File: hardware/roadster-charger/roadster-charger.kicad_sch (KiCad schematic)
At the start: 54 parts, among them J1 USB4505-03-0-A, J2 USB4505-03-0-A, J3 54-00166, Q1 CSD19532Q5B, U1 FUSB307BMPX, U10 OPA340NA, U11 LM75B, U2 ESP32-C3-MINI-1, U3 INA168, U4 LM5050-1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

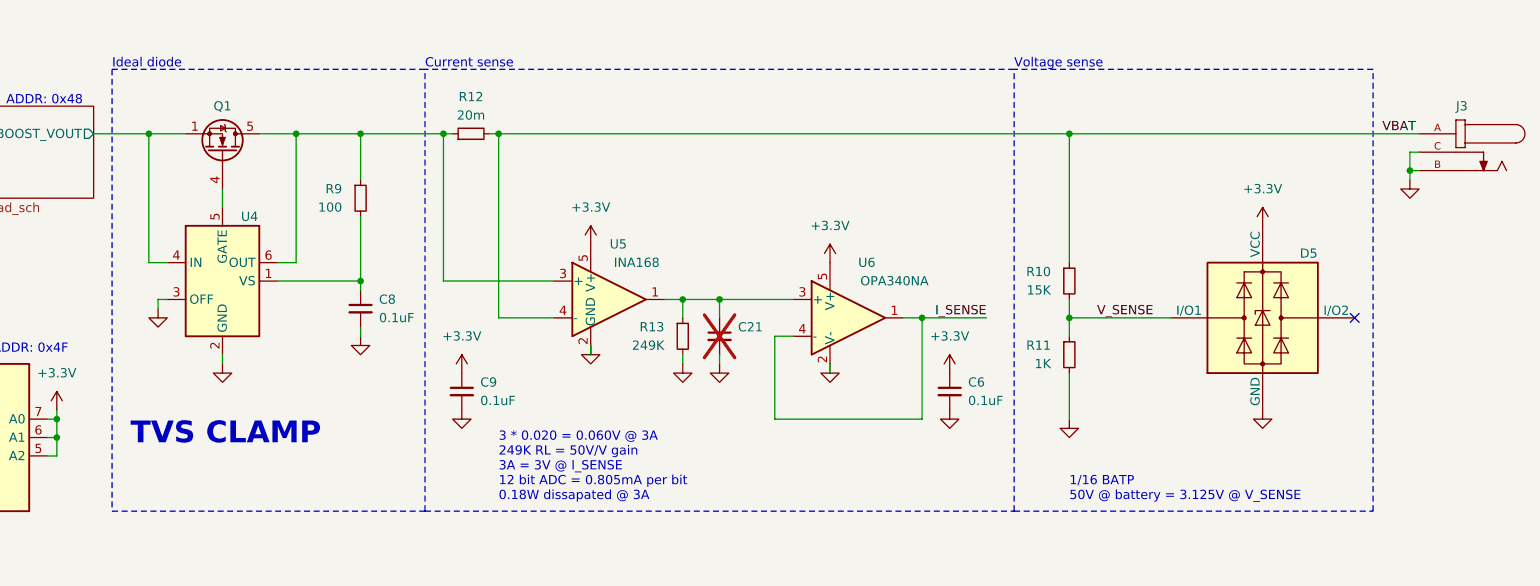
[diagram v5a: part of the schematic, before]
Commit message: add output transient suppressor
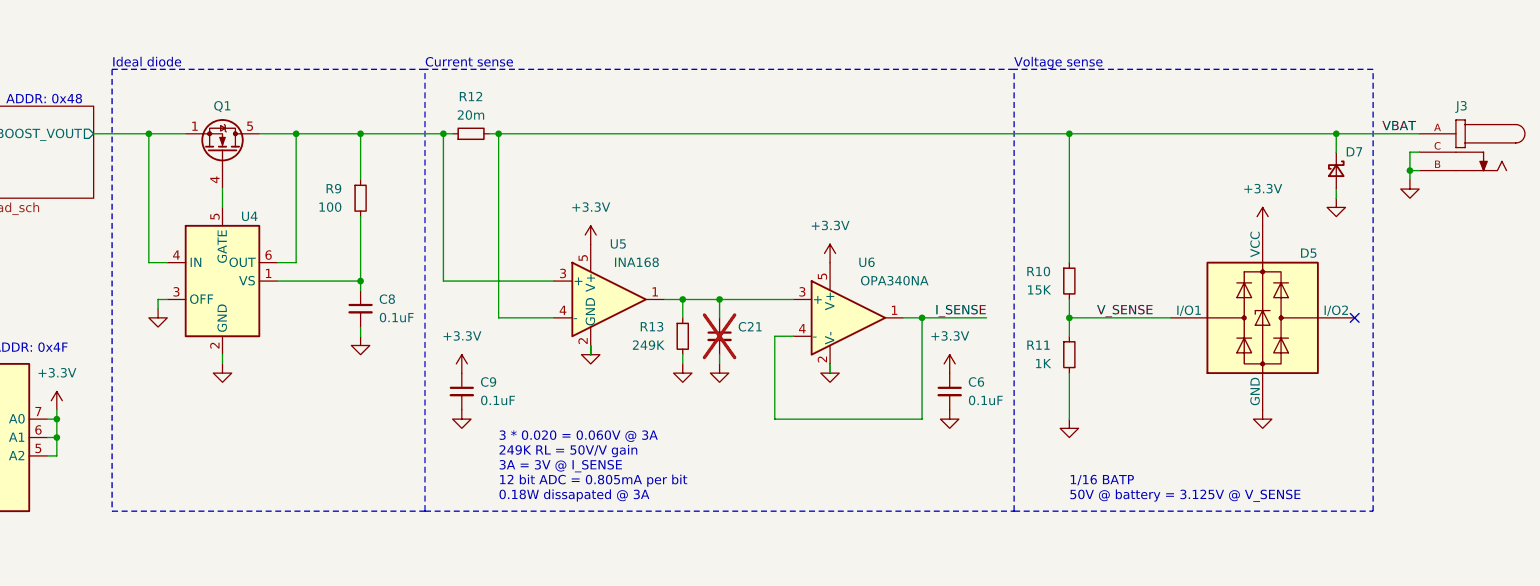
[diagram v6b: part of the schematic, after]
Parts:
- added D7: D_Schottky_Small, Diode_SMD:D_SMB, symbol Device:D_Schottky_Small
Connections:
- net GND: now also D7.2 (A)
- net VBAT: now also D7.1 (K)
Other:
- note removed: "TVS CLAMP"
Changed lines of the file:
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@@
   (junction (at 161.29 138.43) (diameter 0) (color 0 0 0 0)
   )
+  (junction (at 377.19 138.43) (diameter 0) (color 0 0 0 0)
+  )
   (junction (at 290.83 31.75) (diameter 0) (color 0 0 0 0)
   )
@@
     (stroke (width 0) (type default))
   )
+  (wire (pts (xy 377.19 138.43) (xy 388.62 138.43))
+    (stroke (width 0) (type default))
+  )
   (wire (pts (xy 36.83 124.46) (xy 36.83 125.73))
     (stroke (width 0) (type default))
@@
     (stroke (width 0) (type default))
   )
-  (wire (pts (xy 340.36 138.43) (xy 388.62 138.43))
+  (wire (pts (xy 340.36 138.43) (xy 377.19 138.43))
     (stroke (width 0) (type default))
   )
@@
     (stroke (width 0) (type default))
   )
+  (wire (pts (xy 377.19 138.43) (xy 377.19 140.97))
+    (stroke (width 0) (type default))
+  )
   (wire (pts (xy 96.52 222.25) (xy 109.22 222.25))
     (stroke (width 0) (type default))
@@
     (stroke (width 0) (type default))
   )
+  (wire (pts (xy 377.19 146.05) (xy 377.19 147.32))
+    (stroke (width 0) (type default))
+  )
   (wire (pts (xy 292.1 63.5) (xy 292.1 66.04))
     (stroke (width 0) (type default))
@@
     (effects (font (size 1.27 1.27)) (justify left bottom))
   )
-  (text "TVS CLAMP" (at 210.82 181.61 0)
-    (effects (font (size 3 3) (thickness 0.6) bold (color 255 22 22 1)) (justify left bottom))
-  )
   (text "1/16 BATP\n50V @ battery = 3.125V @ V_SENSE" (at 340.36 189.23 0)
     (effects (font (size 1.27 1.27)) (justify left bottom))
@@
     )
   )
+  (symbol (lib_id "power:GND") (at 377.19 147.32 0) (unit 1)
+    (in_bom yes) (on_board yes) (dnp no)
+    (property "Reference" "#PWR079" (at 377.19 153.67 0)
+      (effects (font (size 1.27 1.27)) hide)
+    )
+    (property "Value" "GND" (at 377.19 152.4 0)
+      (effects (font (size 1.27 1.27)) hide)
+    )
+    (property "Footprint" "" (at 377.19 147.32 0)
+      (effects (font (size 1.27 1.27)) hide)
+    )
+    (property "Datasheet" "" (at 377.19 147.32 0)
+      (effects (font (size 1.27 1.27)) hide)
+    )
+    (pin "1")
+    (instances
+      (project "roadster-charger"
+        (path "/57ecac41-cd8a-4182-a81e-fed3e381aedd"
+          (reference "#PWR079") (unit 1)
+        )
+        (path "/57ecac41-cd8a-4182-a81e-fed3e381aedd/64ca4e4e-11ba-4e5c-8f8e-2432a1d47dd0"
+          (reference "#PWR028") (unit 1)
+        )
+      )
+    )
+  )
   (symbol (lib_id "Sensor_Temperature:LM75B") (at 189.23 180.34 0) (unit 1)
     (in_bom yes) (on_board yes) (dnp no)
@@
         )
       )
+    )
+  )
+  (symbol (lib_id "Device:D_Schottky_Small") (at 377.19 143.51 270) (unit 1)
+    (in_bom yes) (on_board yes) (dnp no)
+    (property "Reference" "D7" (at 378.46 140.97 90)
+      (effects (font (size 1.27 1.27)) (justify left))
+    )
+    (property "Value" "D_Schottky_Small" (at 379.73 144.526 90)
+      (effects (font (size 1.27 1.27)) (justify left) hide)
+    )
+    (property "Footprint" "Diode_SMD:D_SMB" (at 377.19 143.51 90)
+      (effects (font (size 1.27 1.27)) hide)
+    )
+    (property "Datasheet" "~" (at 377.19 143.51 90)
+      (effects (font (size 1.27 1.27)) hide)
+    )
+    (property "MPN" "SMBJ60A" (at 377.19 143.51 90)
+      (effects (font (size 1.27 1.27)) hide)
+    )
+    (pin "2")
+    (pin "1")
+    (instances
+      (project "roadster-charger"
+        (path "/57ecac41-cd8a-4182-a81e-fed3e381aedd"
+          (reference "D7") (unit 1)
+        )
+      )

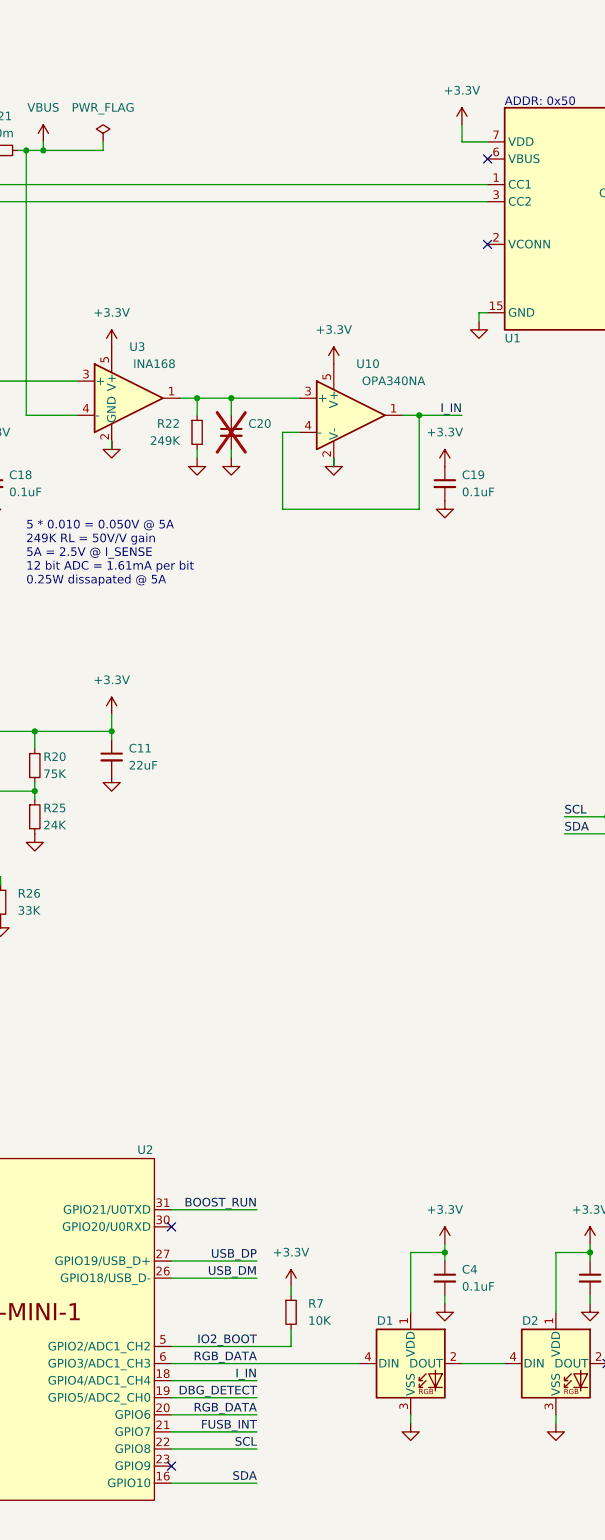
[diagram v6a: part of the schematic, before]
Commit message: correct LED data pin, routing
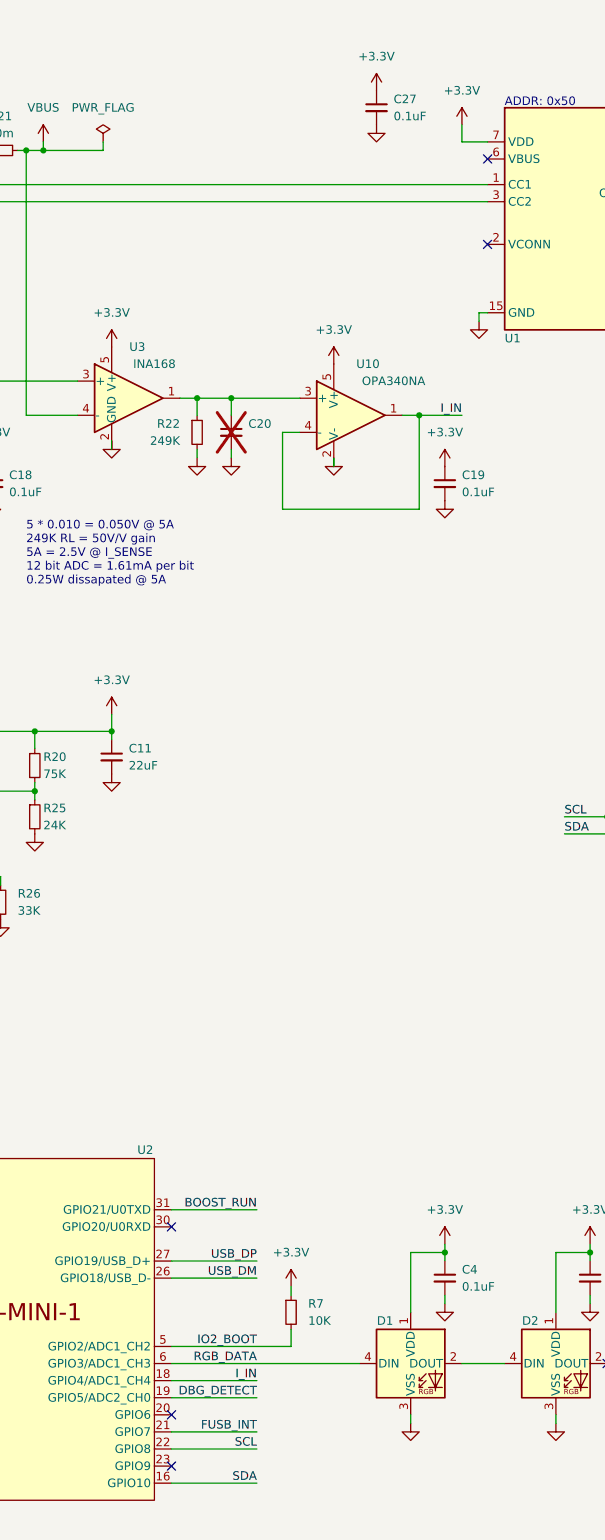
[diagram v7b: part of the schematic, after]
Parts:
- added C27: 0.1uF, Capacitor_SMD:C_0603_1608Metric, symbol Device:C_Small
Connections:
- net +3.3V: now also C27.1
- net GND: now also C27.2
- net RGB_DATA: no longer U2.20 (GPIO6)
- no-connect marks 25 -> 26
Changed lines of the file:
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@@
   (no_connect (at 289.56 43.18))
   (no_connect (at 69.85 140.97))
+  (no_connect (at 96.52 227.33))
   (no_connect (at 289.56 45.72))
   (no_connect (at 161.29 219.71))
@@
     (stroke (width 0) (type default))
   )
-  (wire (pts (xy 96.52 227.33) (xy 109.22 227.33))
-    (stroke (width 0) (type default))
-  )
   (wire (pts (xy 287.02 161.29) (xy 292.1 161.29))
     (stroke (width 0) (type default))
@@
   (label "SCL" (at 181.61 38.1 0) (fields_autoplaced)
     (effects (font (size 1.27 1.27)) (justify left bottom))
-  )
-  (label "RGB_DATA" (at 109.22 227.33 180) (fields_autoplaced)
-    (effects (font (size 1.27 1.27)) (justify right bottom))
   )
   (label "I_IN" (at 139.7 78.74 180) (fields_autoplaced)
@@
     )
   )
+  (symbol (lib_id "Device:C_Small") (at 127 33.02 0) (mirror y) (unit 1)
+    (in_bom yes) (on_board yes) (dnp no)
+    (property "Reference" "C27" (at 129.54 31.7563 0)
+      (effects (font (size 1.27 1.27)) (justify right))
+    )
+    (property "Value" "0.1uF" (at 129.54 34.2963 0)
+      (effects (font (size 1.27 1.27)) (justify right))
+    )
+    (property "Footprint" "Capacitor_SMD:C_0603_1608Metric" (at 127 33.02 0)
+      (effects (font (size 1.27 1.27)) hide)
+    )
+    (property "Datasheet" "~" (at 127 33.02 0)
+      (effects (font (size 1.27 1.27)) hide)
+    )
+    (property "MPN" "CL10B104KB8NNNC" (at 127 33.02 0)
+      (effects (font (size 1.27 1.27)) hide)
+    )
+    (pin "1")
+    (pin "2")
+    (instances
+      (project "roadster-charger"
+        (path "/57ecac41-cd8a-4182-a81e-fed3e381aedd"
+          (reference "C27") (unit 1)
+        )
+      )
+    )
+  )
   (symbol (lib_id "power:GND") (at 242.57 166.37 0) (unit 1)
     (in_bom yes) (on_board yes) (dnp no)
@@
     )
   )
+  (symbol (lib_id "power:GND") (at 127 35.56 0) (unit 1)
+    (in_bom yes) (on_board yes) (dnp no)
+    (property "Reference" "#PWR081" (at 127 41.91 0)
+      (effects (font (size 1.27 1.27)) hide)
+    )
+    (property "Value" "GND" (at 127 40.64 0)
+      (effects (font (size 1.27 1.27)) hide)
+    )
+    (property "Footprint" "" (at 127 35.56 0)
+      (effects (font (size 1.27 1.27)) hide)
+    )
+    (property "Datasheet" "" (at 127 35.56 0)
+      (effects (font (size 1.27 1.27)) hide)
+    )
+    (pin "1")
+    (instances
+      (project "roadster-charger"
+        (path "/57ecac41-cd8a-4182-a81e-fed3e381aedd"
+          (reference "#PWR081") (unit 1)
+        )
+      )
+    )
+  )
   (symbol (lib_id "power:+3.3V") (at 374.65 27.94 0) (unit 1)
     (in_bom yes) (on_board yes) (dnp no) (fields_autoplaced)
@@
         )
       )
+    )
+  )
+  (symbol (lib_id "power:+3.3V") (at 127 30.48 0) (unit 1)
+    (in_bom yes) (on_board yes) (dnp no) (fields_autoplaced)
+    (property "Reference" "#PWR080" (at 127 34.29 0)
+      (effects (font (size 1.27 1.27)) hide)
+    )
+    (property "Value" "+3.3V" (at 127 25.4 0)
+      (effects (font (size 1.27 1.27)))
+    )
+    (property "Footprint" "" (at 127 30.48 0)
+      (effects (font (size 1.27 1.27)) hide)
+    )
+    (property "Datasheet" "" (at 127 30.48 0)
+      (effects (font (size 1.27 1.27)) hide)
+    )
+    (pin "1")
+    (instances
+      (project "roadster-charger"
+        (path "/57ecac41-cd8a-4182-a81e-fed3e381aedd"
+          (reference "#PWR080") (unit 1)
+        )
+      )

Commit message: cleanup
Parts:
- added H1, H2: MountingHole, MountingHole:MountingHole_3.2mm_M3_ISO7380_Pad_TopBottom, symbol Mechanical:MountingHole
- added TP1, TP2, TP3, TP4: TestPoint, RCU-0C:TP+195X110, symbol Connector:TestPoint
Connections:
- net GND: now also TP3.1
- net RGB_DATA: now also TP4.1
- net SCL: now also TP2.1
- net SDA: now also TP1.1
- net V_SW: now reaches U9.4 (SW), U9.5 (SW), U9.6 (SW)
- no-connect marks 26 -> 25
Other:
- moved on the sheet: R2, R20, R25, R3, R4
